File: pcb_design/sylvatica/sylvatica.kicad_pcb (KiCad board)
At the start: 2 copper layers, 93 x 93 mm, 120 parts, among them J1 USB_C_Receptacle, J2 USB_C_Receptacle, J3 USB_C_Receptacle, J4 USB_C_Receptacle, J5 Conn_02x13_Odd_Even, J6 Conn_01x04_Female, J7 Conn_01x06_Female, J9 Conn_01x06_Female, Q1 Q_NMOS_GSD, Q2 Q_NMOS_GSD, SW1 SW_Push, U1 PGA113, U10 dsPIC33EP512MC806, U11 SiP32431, U12 LP2985-5.0, U13 REF2033, U14 OPA320, U15 SiP32431, U16 SiP32431, U17 SiP32431, U18 SiP32431, U19 ADM7170, U2 PGA113, U20 MCP2542FD, U21 TPS737, U22 SiP32431, U3 PGA113, U4 PGA113, U5 PGA113, U6 PGA113, U7 PGA113, U8 PGA113, U9 ADS8332, Y1 Crystal_GND24

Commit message: Update.
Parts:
- added J8: Conn_01x04_Female, Connector_PinSocket_2.54mm:PinSocket_1x04_P2.54mm_Vertical, F.Cu at (52.0, 57.0)
- moved D1 100.6 mm to (56.3, 129.3), turned to 90 degrees
- moved R17 95.0 mm to (56.3, 126.0), turned to 90 degrees
- moved D2 87.2 mm to (113.7, 129.4), turned to 90 degrees
- moved R18 80.6 mm to (113.7, 126.1), turned to 90 degrees
- moved C22 16.5 mm to (65.7, 47.5), turned to -90 degrees
- moved R36 9.45 mm to (62.3, 47.5)
- moved R19 8.65 mm to (64.0, 47.5), turned to 90 degrees
- moved R7 8.05 mm to (114.6, 51.4)
- moved C58 8.05 mm to (105.5, 47.2)
- moved C59 8.05 mm to (114.6, 53.3)
- moved U21 8.05 mm to (110.5, 45.7)
- moved C60 7.94 mm to (109.3, 52.7)
- moved R34 7.02 mm to (90.0, 111.4)
- moved J9 7.00 mm to (52.0, 52.0)
- moved SW1 6.16 mm to (58.6, 47.5)
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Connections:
- net +3V3 renamed +3.3V
- net /AS_PS renamed /S_PS
- net /AS_PS2 renamed /S_PS2
- J1 pad A10: /EV1 -> /SCL1
- J1 pad A11: Net-(J1-PadA11) -> unconnected-(J1-PadA11)
- J1 pad A3: /OW1 -> /SDA1
- J1 pad A5: Net-(J1-PadA5) -> unconnected-(J1-PadA5)
- J1 pad A6: /SDA1 -> /OW1
- J1 pad A7: /SCL1 -> /EV1
- J1 pad A8: Net-(J1-PadA8) -> unconnected-(J1-PadA8)
- J1 pad B10: /EV1 -> /SCL1
- J1 pad B11: Net-(J1-PadB11) -> unconnected-(J1-PadB11)
- J1 pad B3: /OW1 -> /SDA1
- J1 pad B5: Net-(J1-PadB5) -> unconnected-(J1-PadB5)
- J1 pad B6: /SDA1 -> /OW1
- J1 pad B7: /SCL1 -> /EV1
- J1 pad B8: Net-(J1-PadB8) -> unconnected-(J1-PadB8)
- J2 pad A10: /EV2 -> /SCL1
- J2 pad A11: Net-(J2-PadA11) -> unconnected-(J2-PadA11)
- J2 pad A3: /OW2 -> /SDA1
- J2 pad A5: Net-(J2-PadA5) -> unconnected-(J2-PadA5)
- J2 pad A6: /SDA1 -> /OW2
- J2 pad A7: /SCL1 -> /EV2
- J2 pad A8: Net-(J2-PadA8) -> unconnected-(J2-PadA8)
- J2 pad B10: /EV2 -> /SCL1
- J2 pad B11: Net-(J2-PadB11) -> unconnected-(J2-PadB11)
- J2 pad B3: /OW2 -> /SDA1
- J2 pad B5: Net-(J2-PadB5) -> unconnected-(J2-PadB5)
- J2 pad B6: /SDA1 -> /OW2
- J2 pad B7: /SCL1 -> /EV2
- J2 pad B8: Net-(J2-PadB8) -> unconnected-(J2-PadB8)
- J3 pad A10: /EV3 -> /SCL1
- J3 pad A11: Net-(J3-PadA11) -> unconnected-(J3-PadA11)
- J3 pad A3: /OW3 -> /SDA1
- J3 pad A5: Net-(J3-PadA5) -> unconnected-(J3-PadA5)
- J3 pad A6: /SDA1 -> /OW3
- J3 pad A7: /SCL1 -> /EV3
- J3 pad A8: Net-(J3-PadA8) -> unconnected-(J3-PadA8)
- J3 pad B10: /EV3 -> /SCL1
- J3 pad B11: Net-(J3-PadB11) -> unconnected-(J3-PadB11)
- J3 pad B3: /OW3 -> /SDA1
- J3 pad B5: Net-(J3-PadB5) -> unconnected-(J3-PadB5)
- J3 pad B6: /SDA1 -> /OW3
- J3 pad B7: /SCL1 -> /EV3
- J3 pad B8: Net-(J3-PadB8) -> unconnected-(J3-PadB8)
- J4 pad A10: /EV4 -> /SCL1
- J4 pad A11: Net-(J4-PadA11) -> unconnected-(J4-PadA11)
- J4 pad A3: /OW4 -> /SDA1
- J4 pad A5: Net-(J4-PadA5) -> unconnected-(J4-PadA5)
- J4 pad A6: /SDA1 -> /OW4
- J4 pad A7: /SCL1 -> /EV4
- J4 pad A8: Net-(J4-PadA8) -> unconnected-(J4-PadA8)
- J4 pad B10: /EV4 -> /SCL1
- J4 pad B11: Net-(J4-PadB11) -> unconnected-(J4-PadB11)
- J4 pad B3: /OW4 -> /SDA1
- J4 pad B5: Net-(J4-PadB5) -> unconnected-(J4-PadB5)
- J4 pad B6: /SDA1 -> /OW4
- J4 pad B7: /SCL1 -> /EV4
- J4 pad B8: Net-(J4-PadB8) -> unconnected-(J4-PadB8)
- J5 pad 12: Net-(J5-Pad12) -> unconnected-(J5-Pad12)
- J5 pad 14: /OW5 -> unconnected-(J5-Pad14)
- J5 pad 16: Net-(J5-Pad16) -> unconnected-(J5-Pad16)
- J5 pad 18: /OW6 -> unconnected-(J5-Pad18)
- J5 pad 19: Net-(J5-Pad19) -> unconnected-(J5-Pad19)
- J5 pad 20: Net-(J5-Pad20) -> unconnected-(J5-Pad20)
- J5 pad 21: Net-(J5-Pad21) -> unconnected-(J5-Pad21)
- J5 pad 22: /OW7 -> unconnected-(J5-Pad22)
- J5 pad 23: /CAN_C1 -> unconnected-(J5-Pad23)
- J5 pad 24: Net-(J5-Pad24) -> unconnected-(J5-Pad24)
- J5 pad 25: Net-(J5-Pad25) -> unconnected-(J5-Pad25)
- J5 pad 26: /OW8 -> GND
- J5 pad 3: Net-(J5-Pad3) -> GND
- J5 pad 6: Net-(J5-Pad6) -> GND
- J5 pad 8: Net-(J5-Pad8) -> unconnected-(J5-Pad8)
- J9 pad 6: /PGM -> unconnected-(J9-Pad6)
- U10 pad 11: Net-(U10-Pad11) -> /OW3
- U10 pad 12: /S_PS_SW2 -> /OW7
- U10 pad 13: /~{INT2} -> /OW8
- U10 pad 15: Net-(U10-Pad15) -> /S_PS_SW2
- U10 pad 16: Net-(U10-Pad16) -> /~{INT2}
- U10 pad 21: Net-(U10-Pad21) -> /OW2
- U10 pad 22: Net-(U10-Pad22) -> /OW1
- U10 pad 23: Net-(U10-Pad23) -> /OW5
- U10 pad 27: Net-(U10-Pad27) -> /REF_C2
- U10 pad 28: Net-(U10-Pad28) -> /OW6
- U10 pad 29: /REF_C2 -> unconnected-(U10-Pad29)
- U10 pad 63: Net-(U10-Pad63) -> /BLINK
- U10 pad 64: /BLINK -> /OW4
- U10 pad 8: Net-(U10-Pad8) -> unconnected-(U10-Pad8)
- U11 pad 6: Net-(U11-Pad6) -> unconnected-(U11-Pad6)
- U15 pad 6: Net-(U15-Pad6) -> unconnected-(U15-Pad6)
- U16 pad 6: Net-(U16-Pad6) -> unconnected-(U16-Pad6)
- U17 pad 6: Net-(U17-Pad6) -> unconnected-(U17-Pad6)
- U18 pad 6: Net-(U18-Pad6) -> unconnected-(U18-Pad6)
- U22 pad 6: Net-(U22-Pad6) -> unconnected-(U22-Pad6)
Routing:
- net /OW3: track 12.5 -> 162.6 mm, vias 2 -> 7
- net /OW2: track 12.9 -> 142.1 mm, vias 2 -> 4
- net /OW4: track 12.4 -> 127.2 mm, vias 2 -> 5
- net /OW1: track 12.5 -> 122.6 mm, vias 2 -> 4
- net /BLINK: track 37.0 -> 108.5 mm, vias 4 -> 2
- net /SCL1: track 148.9 -> 189.2 mm, vias 8 -> 14
- net /OW6: track 0.00 -> 40.0 mm, vias 0 -> 3
- net /OW5: track 0.00 -> 36.4 mm, vias 0 -> 1
- net /OW7: track 0.00 -> 32.7 mm, vias 0 -> 1
- net /OW8: track 0.00 -> 29.1 mm
- net /SDA1: track 165.8 -> 192.7 mm
- net GND: track 183.4 -> 162.2 mm, vias 81 -> 83
- net +3.3V: track 405.2 -> 419.5 mm, vias 18 -> 26
- net VBUS: track 151.5 -> 137.5 mm
- net /~{CS2}: track 88.6 -> 101.9 mm
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- removed copper zone on F.Cu, net /SCL1
- removed copper zone on F.Cu, net /S_PS
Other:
- rule pad_to_mask_clearance: 0.051 -> 0
- board text added: "Gloxinia sylvatica rev. 7"
- board text added: "PWR"
- board text added: "STATUS"
- board text removed: "gloxinia system"

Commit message: New and updated board designs.
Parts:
- removed J7: Conn_01x06_Female, Connector_PinSocket_2.54mm:PinSocket_1x06_P2.54mm_Vertical
- removed J8: Conn_01x04_Female, Connector_PinSocket_2.54mm:PinSocket_1x04_P2.54mm_Vertical
- removed R16: 10k, Resistor_SMD:R_0603_1608Metric
- added C63: 4.7nF, Capacitor_SMD:C_0603_1608Metric, F.Cu at (102.8, 47.4)
- added R11: 60R, Resistor_SMD:R_0603_1608Metric, F.Cu at (103.5, 51.2)
- added R8: 1k, Resistor_SMD:R_0603_1608Metric, F.Cu at (98.3, 52.8)
- J5: value Conn_02x13_Odd_Even -> Conn_02x07_Odd_Even; footprint Connector_PinHeader_2.54mm:PinHeader_2x13_P2.54mm_Vertical -> samtec:SAMTEC_TMMH-107-01-T-DV; moved to B.Cu
- J6: value Conn_01x04_Female -> Conn_02x07_Odd_Even; footprint Connector_PinSocket_2.54mm:PinSocket_1x04_P2.54mm_Vertical -> samtec:SAMTEC_TMMH-107-01-T-DV
- N1: footprint board:Enclosure-Gloxinia2 -> board:Enclosure-Gloxinia4
- R15: value 10k -> 60R
- moved R15 61.1 mm to (103.5, 49.6), turned to 180 degrees
- moved Q2 56.6 mm to (100.2, 50.0)
- moved C43 37.4 mm to (51.1, 60.4)
- moved C48 37.1 mm to (65.1, 60.4)
- moved C51 37.1 mm to (55.9, 60.4)
- moved C52 37.1 mm to (59.1, 60.4)
- moved U17 37.1 mm to (53.4, 60.4)
- moved U18 37.1 mm to (62.1, 60.4)
- moved J6 20.5 mm to (54.0, 101.0)
- moved J5 15.0 mm to (85.0, 45.0), turned to 180 degrees
- moved C49 9.59 mm to (108.3, 103.7), turned to 90 degrees
- moved U11 6.09 mm to (111.1, 103.7), turned to 90 degrees
- moved C53 6.00 mm to (117.8, 96.2)
- moved C54 6.00 mm to (120.2, 92.8)
- moved C55 6.00 mm to (117.8, 88.5)
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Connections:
- J5 pad 10: /~{INT2} -> +3.3V
- J5 pad 11: /CAN_L -> GND
- J5 pad 12: unconnected-(J5-Pad12) -> GND
- J5 pad 13: /SDA2 -> GND
- J5 pad 14: unconnected-(J5-Pad14) -> GND
- J5 pad 2: VBUS -> /RTS
- J5 pad 3: GND -> /CAN_H
- J5 pad 4: VBUS -> /CTS
- J5 pad 5: /CAN_H -> /CAN_L
- J5 pad 6: GND -> /TXD
- J5 pad 7: /CAN_H -> /CAN_C1
- J5 pad 8: unconnected-(J5-Pad8) -> /RXD
- J5 pad 9: /CAN_L -> /CAN_C2
- J6 pad 1: /EV5 -> /S_PS2
- J6 pad 2: /EV6 -> GND
- J6 pad 3: /EV7 -> /SCL2
- J6 pad 4: /EV8 -> GND
- Q2 pad 1: +3.3V -> Net-(Q2-Pad1)
- Q2 pad 2: /EN_REF -> Net-(Q2-Pad2)
- Q2 pad 3: /EN_REF3.3 -> /CAN_H
- R15 pad 1: +3.3V -> /CAN_L
- R15 pad 2: /EN_REF -> Net-(C63-Pad1)
- U10 pad 14: /AS_PS_SW2 -> /CAN_C2
- U10 pad 16: /~{INT2} -> /AS_PS_SW2
- U10 pad 23: /OW5 -> /~{INT2}
- U10 pad 24: /EN_REF -> /TERM
- U10 pad 29: unconnected-(U10-Pad29) -> /OW5
- U10 pad 8: unconnected-(U10-Pad8) -> /CAN_C1
- U13 pad 3: /EN_REF3.3 -> +4V
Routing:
- net /OW8: track 29.1 -> 101.2 mm, vias 0 -> 2
- net /OW7: track 32.7 -> 97.0 mm, vias 1 -> 2
- net /~{INT2}: track 25.3 -> 89.3 mm, vias 1 -> 4
- net /S_PS2: track 13.4 -> 74.5 mm, vias 0 -> 2
- net /EN_REF: track 41.8 -> 0.00 mm, vias 2 -> 0
- net /OW5: track 36.4 -> 73.1 mm, vias 1 -> 4
- net /SDA2: track 43.8 -> 80.2 mm
- net /OW6: track 40.0 -> 73.2 mm, vias 3 -> 6
- net /SCL2: track 44.2 -> 76.4 mm
- net /CAN_L: track 16.2 -> 45.2 mm, vias 0 -> 2
- net /TERM: track 0.00 -> 28.9 mm, vias 0 -> 6
- net /CAN_H: track 11.6 -> 39.8 mm, vias 0 -> 5
- net VBUS: track 137.5 -> 114.2 mm, vias 2 -> 4
- net /CAN_C1: track 0.00 -> 23.1 mm, vias 0 -> 1
- net /CAN_C2: track 0.00 -> 20.0 mm, vias 0 -> 1
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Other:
- outline, holes or cut-outs redrawn
- board text added: "Gloxinia sylvatica rev. 8"
- board text removed: "Gloxinia sylvatica rev. 7"

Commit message: Expose RTCC pin for synchronisation
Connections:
- J5 pad 10: +3.3V -> /~{INT1}
- J5 pad 12: GND -> +3.3V
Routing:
- net /~{INT1}: track 212.5 -> 277.2 mm, vias 15 -> 20
- net +3.3V: track 433.9 -> 431.1 mm
- net /~{CS2}: track 101.0 -> 99.6 mm
- net /SCL1: track 185.8 -> 186.7 mm
- net /SCK_PGA: track 191.6 -> 190.6 mm
- net /SDA1: track 189.1 -> 189.8 mm
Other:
- board text added: "Gloxinia sylvatica rev. 9"
- board text removed: "Gloxinia sylvatica rev. 8"

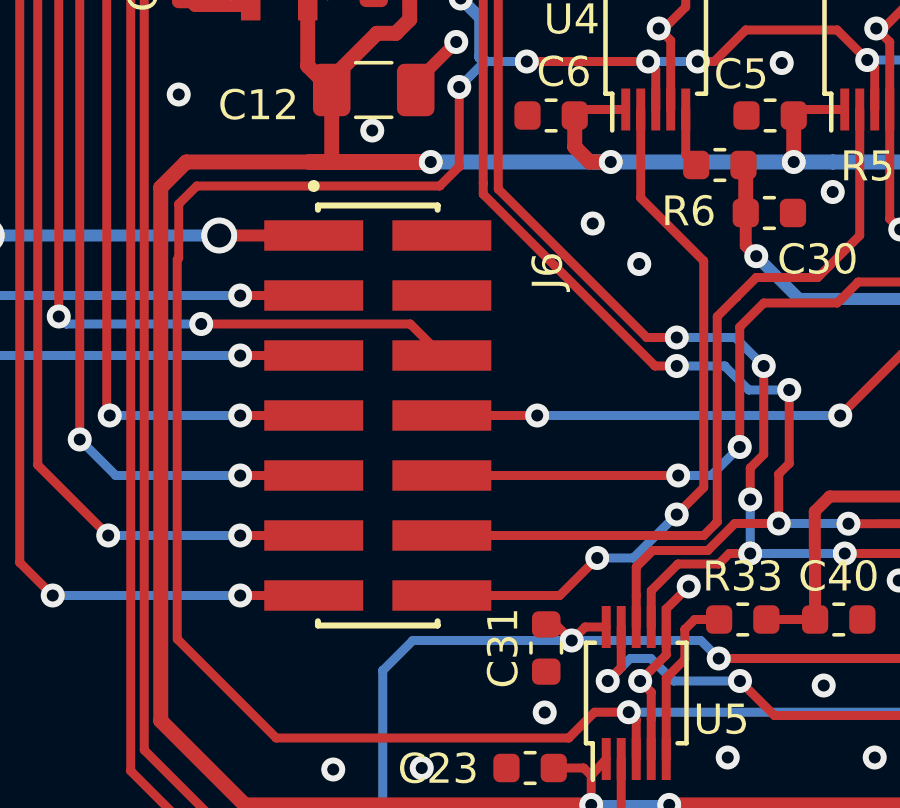
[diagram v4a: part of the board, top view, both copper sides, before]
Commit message: Bug fix in component layout
Connector was not updated to latest version, resulting in mis alignment w.r.t. connector board.
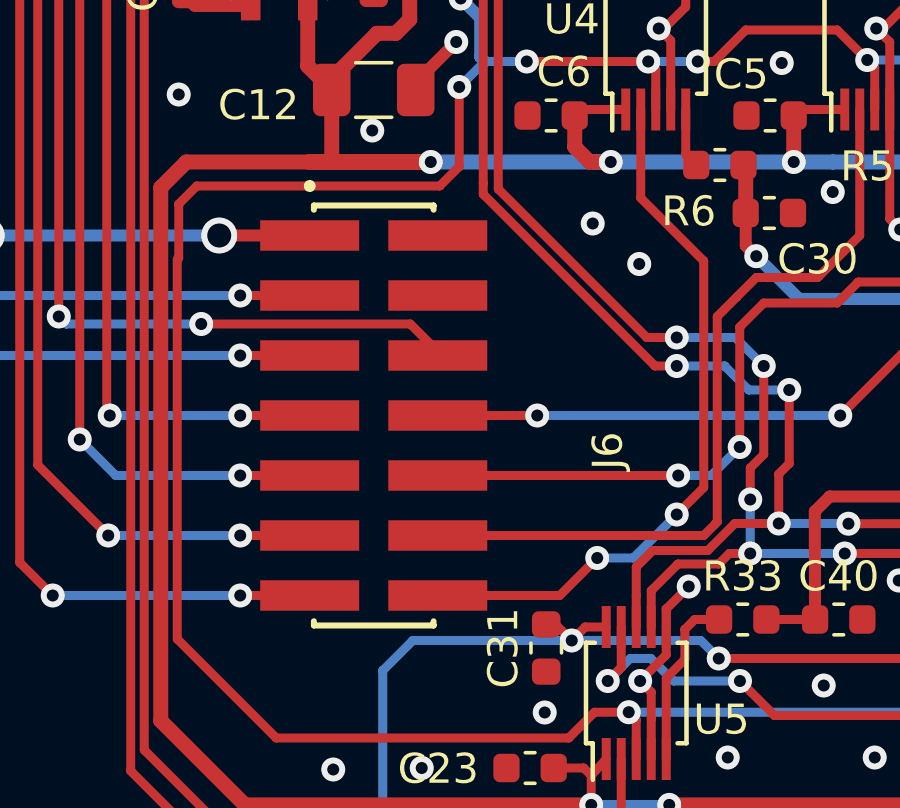
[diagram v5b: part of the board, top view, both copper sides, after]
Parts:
- moved J6 6.32 mm to (56.0, 107.0)
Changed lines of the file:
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@@
   )
   (footprint "samtec:SAMTEC_TMMH-107-01-T-DV" (layer "F.Cu")
-    (at 54 101 -90)
+    (at 56 107 -90)
     (property "Sheetfile" "sylvatica.kicad_sch")
     (property "Sheetname" "")
@@
       (effects (font (size 1 1) (thickness 0.15)))
     )
-    (fp_line (start 12.858 -0.14) (end 13 -0.14) (layer "F.SilkS") (width 0.2))
-    (fp_line (start -0.858 -0.14) (end -1 -0.14) (layer "F.SilkS") (width 0.2))
-    (fp_line (start 12.858 -4.13) (end 13 -4.13) (layer "F.SilkS") (width 0.2))
-    (fp_line (start -1 -0.14) (end -1 -4.13) (layer "F.SilkS") (width 0.2))
-    (fp_line (start 13 -4.13) (end 13 -0.14) (layer "F.SilkS") (width 0.2))
-    (fp_line (start -1 -4.13) (end -0.858 -4.13) (layer "F.SilkS") (width 0.2))
-    (fp_circle (center -1.65 0) (end -1.55 0) (layer "F.SilkS") (width 0.2) (fill none))
-    (fp_line (start 13.25 1.9) (end -1.25 1.9) (layer "F.CrtYd") (width 0.05))
-    (fp_line (start -1.25 -6.169) (end 13.25 -6.169) (layer "F.CrtYd") (width 0.05))
-    (fp_line (start -1.25 1.9) (end -1.25 -6.169) (layer "F.CrtYd") (width 0.05))
-    (fp_line (start 13.25 -6.169) (end 13.25 1.9) (layer "F.CrtYd") (width 0.05))
-    (fp_line (start -1 -0.14) (end -1 -4.13) (layer "F.Fab") (width 0.1))
-    (fp_line (start -1 -4.13) (end 13 -4.13) (layer "F.Fab") (width 0.1))
-    (fp_line (start 13 -4.13) (end 13 -0.14) (layer "F.Fab") (width 0.1))
-    (fp_line (start 13 -0.14) (end -1 -0.14) (layer "F.Fab") (width 0.1))
-    (fp_circle (center -1.65 0) (end -1.55 0) (layer "F.Fab") (width 0.2) (fill none))
-    (pad "1" smd rect (at 0 0 270) (size 1.016 3.3) (layers "F.Cu" "F.Paste" "F.Mask")
+    (fp_line (start 6.858 1.995) (end 7 1.995) (layer "F.SilkS") (width 0.2))
+    (fp_line (start -6.858 1.995) (end -7 1.995) (layer "F.SilkS") (width 0.2))
+    (fp_line (start 7 -1.995) (end 7 1.995) (layer "F.SilkS") (width 0.2))
+    (fp_line (start 6.858 -1.995) (end 7 -1.995) (layer "F.SilkS") (width 0.2))
+    (fp_line (start -7 1.995) (end -7 -1.995) (layer "F.SilkS") (width 0.2))
+    (fp_line (start -7 -1.995) (end -6.858 -1.995) (layer "F.SilkS") (width 0.2))
+    (fp_circle (center -7.65 2.135) (end -7.55 2.135) (layer "F.SilkS") (width 0.2) (fill none))
+    (fp_line (start 7.25 4.035) (end -7.25 4.035) (layer "F.CrtYd") (width 0.05))
+    (fp_line (start 7.25 -4.034) (end 7.25 4.035) (layer "F.CrtYd") (width 0.05))
+    (fp_line (start -7.25 -4.034) (end 7.25 -4.034) (layer "F.CrtYd") (width 0.05))
+    (fp_line (start -7.25 4.035) (end -7.25 -4.034) (layer "F.CrtYd") (width 0.05))
+    (fp_line (start 7 1.995) (end -7 1.995) (layer "F.Fab") (width 0.1))
+    (fp_line (start -7 1.995) (end -7 -1.995) (layer "F.Fab") (width 0.1))
+    (fp_line (start 7 -1.995) (end 7 1.995) (layer "F.Fab") (width 0.1))
+    (fp_line (start -7 -1.995) (end 7 -1.995) (layer "F.Fab") (width 0.1))
+    (fp_circle (center -7.65 2.135) (end -7.55 2.135) (layer "F.Fab") (width 0.2) (fill none))
+    (pad "1" smd rect (at -6 2.135 270) (size 1.016 3.3) (layers "F.Cu" "F.Paste" "F.Mask")
       (net 50 "/S_PS2") (pinfunction "Pin_1") (pintype "passive"))
-    (pad "2" smd rect (at 0 -4.269 270) (size 1.016 3.3) (layers "F.Cu" "F.Paste" "F.Mask")
+    (pad "2" smd rect (at -6 -2.134 270) (size 1.016 3.3) (layers "F.Cu" "F.Paste" "F.Mask")
       (net 34 "GND") (pinfunction "Pin_2") (pintype "passive"))
-    (pad "3" smd rect (at 2 0 270) (size 1.016 3.3) (layers "F.Cu" "F.Paste" "F.Mask")
+    (pad "3" smd rect (at -4 2.135 270) (size 1.016 3.3) (layers "F.Cu" "F.Paste" "F.Mask")
       (net 129 "/SCL2") (pinfunction "Pin_3") (pintype "passive"))
-    (pad "4" smd rect (at 2 -4.269 270) (size 1.016 3.3) (layers "F.Cu" "F.Paste" "F.Mask")
+    (pad "4" smd rect (at -4 -2.134 270) (size 1.016 3.3) (layers "F.Cu" "F.Paste" "F.Mask")
       (net 34 "GND") (pinfunction "Pin_4") (pintype "passive"))
-    (pad "5" smd rect (at 4 0 270) (size 1.016 3.3) (layers "F.Cu" "F.Paste" "F.Mask")
+    (pad "5" smd rect (at -2 2.135 270) (size 1.016 3.3) (layers "F.Cu" "F.Paste" "F.Mask")
       (net 130 "/SDA2") (pinfunction "Pin_5") (pintype "passive"))
-    (pad "6" smd rect (at 4 -4.269 270) (size 1.016 3.3) (layers "F.Cu" "F.Paste" "F.Mask")
+    (pad "6" smd rect (at -2 -2.134 270) (size 1.016 3.3) (layers "F.Cu" "F.Paste" "F.Mask")
       (net 131 "/~{INT2}") (pinfunction "Pin_6") (pintype "passive"))
-    (pad "7" smd rect (at 6 0 270) (size 1.016 3.3) (layers "F.Cu" "F.Paste" "F.Mask")
+    (pad "7" smd rect (at 0 2.135 270) (size 1.016 3.3) (layers "F.Cu" "F.Paste" "F.Mask")
       (net 133 "/OW5") (pinfunction "Pin_7") (pintype "passive"))
-    (pad "8" smd rect (at 6 -4.269 270) (size 1.016 3.3) (layers "F.Cu" "F.Paste" "F.Mask")
+    (pad "8" smd rect (at 0 -2.134 270) (size 1.016 3.3) (layers "F.Cu" "F.Paste" "F.Mask")
       (net 58 "/EV5") (pinfunction "Pin_8") (pintype "passive"))
-    (pad "9" smd rect (at 8 0 270) (size 1.016 3.3) (layers "F.Cu" "F.Paste" "F.Mask")
+    (pad "9" smd rect (at 2 2.135 270) (size 1.016 3.3) (layers "F.Cu" "F.Paste" "F.Mask")
       (net 134 "/OW6") (pinfunction "Pin_9") (pintype "passive"))
-    (pad "10" smd rect (at 8 -4.269 270) (size 1.016 3.3) (layers "F.Cu" "F.Paste" "F.Mask")
+    (pad "10" smd rect (at 2 -2.134 270) (size 1.016 3.3) (layers "F.Cu" "F.Paste" "F.Mask")
       (net 55 "/EV6") (pinfunction "Pin_10") (pintype "passive"))
-    (pad "11" smd rect (at 10 0 270) (size 1.016 3.3) (layers "F.Cu" "F.Paste" "F.Mask")
+    (pad "11" smd rect (at 4 2.135 270) (size 1.016 3.3) (layers "F.Cu" "F.Paste" "F.Mask")
       (net 135 "/OW7") (pinfunction "Pin_11") (pintype "passive"))
-    (pad "12" smd rect (at 10 -4.269 270) (size 1.016 3.3) (layers "F.Cu" "F.Paste" "F.Mask")
+    (pad "12" smd rect (at 4 -2.134 270) (size 1.016 3.3) (layers "F.Cu" "F.Paste" "F.Mask")
       (net 56 "/EV7") (pinfunction "Pin_12") (pintype "passive"))
-    (pad "13" smd rect (at 12 0 270) (size 1.016 3.3) (layers "F.Cu" "F.Paste" "F.Mask")
+    (pad "13" smd rect (at 6 2.135 270) (size 1.016 3.3) (layers "F.Cu" "F.Paste" "F.Mask")
       (net 136 "/OW8") (pinfunction "Pin_13") (pintype "passive"))
-    (pad "14" smd rect (at 12 -4.269 270) (size 1.016 3.3) (layers "F.Cu" "F.Paste" "F.Mask")
+    (pad "14" smd rect (at 6 -2.134 270) (size 1.016 3.3) (layers "F.Cu" "F.Paste" "F.Mask")
       (net 57 "/EV8") (pinfunction "Pin_14") (pintype "passive"))
   )
